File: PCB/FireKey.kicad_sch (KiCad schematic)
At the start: 76 parts, among them SW1 SW_MEC_5E, U1 Arduino_Pro_Micro_USB-C

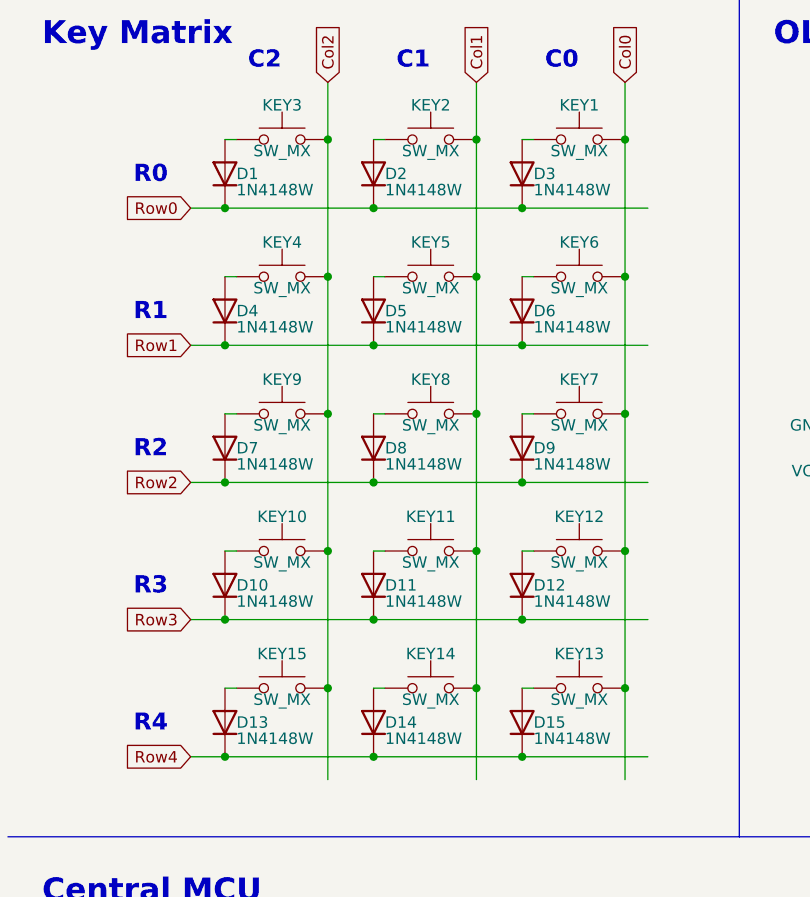
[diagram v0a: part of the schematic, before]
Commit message: fixed diode naming in schematic
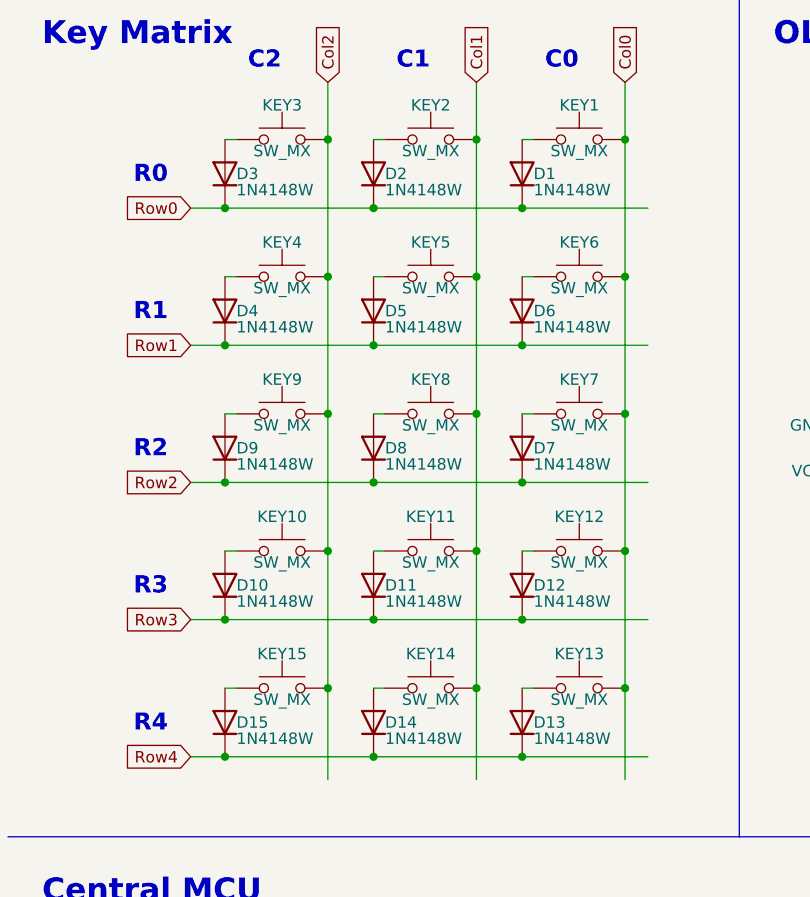
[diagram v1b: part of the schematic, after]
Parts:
- renumbered D3 to D1, D15 to D13, D13 to D15, D1 to D3, D9 to D7, D7 to D9
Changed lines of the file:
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@@
   (symbol (lib_id "Device:D") (at 36.83 64.77 90) (unit 1)
     (in_bom yes) (on_board yes)
-    (property "Reference" "D7" (id 0) (at 38.1 64.77 90)
+    (property "Reference" "D9" (id 0) (at 38.1 64.77 90)
       (effects (font (size 1.27 1.27)) (justify right))
     )
@@
   (symbol (lib_id "Device:D") (at 69.85 64.77 90) (unit 1)
     (in_bom yes) (on_board yes)
-    (property "Reference" "D9" (id 0) (at 71.12 64.77 90)
+    (property "Reference" "D7" (id 0) (at 71.12 64.77 90)
       (effects (font (size 1.27 1.27)) (justify right))
     )
@@
   (symbol (lib_id "Device:D") (at 36.83 95.25 90) (unit 1)
     (in_bom yes) (on_board yes)
-    (property "Reference" "D13" (id 0) (at 38.1 95.25 90)
+    (property "Reference" "D15" (id 0) (at 38.1 95.25 90)
       (effects (font (size 1.27 1.27)) (justify right))
     )
@@
   (symbol (lib_id "Device:D") (at 69.85 34.29 90) (unit 1)
     (in_bom yes) (on_board yes)
-    (property "Reference" "D3" (id 0) (at 71.12 34.29 90)
+    (property "Reference" "D1" (id 0) (at 71.12 34.29 90)
       (effects (font (size 1.27 1.27)) (justify right))
     )
@@
   (symbol (lib_id "Device:D") (at 69.85 95.25 90) (unit 1)
     (in_bom yes) (on_board yes)
-    (property "Reference" "D15" (id 0) (at 71.12 95.25 90)
+    (property "Reference" "D13" (id 0) (at 71.12 95.25 90)
       (effects (font (size 1.27 1.27)) (justify right))
     )
@@
   (symbol (lib_id "Device:D") (at 36.83 34.29 90) (unit 1)
     (in_bom yes) (on_board yes)
-    (property "Reference" "D1" (id 0) (at 38.1 34.29 90)
+    (property "Reference" "D3" (id 0) (at 38.1 34.29 90)
       (effects (font (size 1.27 1.27)) (justify right))
     )
@@
       (reference "C15") (unit 1) (value "100nF") (footprint "Capacitor_SMD:C_0603_1608Metric_Pad1.08x0.95mm_HandSolder")
     )
-    (path "/f34b1302-aa97-4813-9c4e-2a8138dd0fb2"
+    (path "/bfd96171-12af-4791-ab58-317d035aa543"
       (reference "D1") (unit 1) (value "1N4148W") (footprint "Diode_SMD:D_SOD-123")
     )
@@
       (reference "D2") (unit 1) (value "1N4148W") (footprint "Diode_SMD:D_SOD-123")
     )
-    (path "/bfd96171-12af-4791-ab58-317d035aa543"
+    (path "/f34b1302-aa97-4813-9c4e-2a8138dd0fb2"
       (reference "D3") (unit 1) (value "1N4148W") (footprint "Diode_SMD:D_SOD-123")
     )
@@
       (reference "D6") (unit 1) (value "1N4148W") (footprint "Diode_SMD:D_SOD-123")
     )
-    (path "/2c55b189-9010-424a-b20d-57c20a3668f7"
+    (path "/56ad33f8-70ed-48d2-b08e-3210a82c8223"
       (reference "D7") (unit 1) (value "1N4148W") (footprint "Diode_SMD:D_SOD-123")
     )
@@
       (reference "D8") (unit 1) (value "1N4148W") (footprint "Diode_SMD:D_SOD-123")
     )
-    (path "/56ad33f8-70ed-48d2-b08e-3210a82c8223"
+    (path "/2c55b189-9010-424a-b20d-57c20a3668f7"
       (reference "D9") (unit 1) (value "1N4148W") (footprint "Diode_SMD:D_SOD-123")
     )
@@
       (reference "D12") (unit 1) (value "1N4148W") (footprint "Diode_SMD:D_SOD-123")
     )
-    (path "/bb947126-6a07-4e0f-b955-2a81a21f7c79"
+    (path "/c8ff5777-16c4-4cc5-b626-563164697ef6"
       (reference "D13") (unit 1) (value "1N4148W") (footprint "Diode_SMD:D_SOD-123")
     )
@@
       (reference "D14") (unit 1) (value "1N4148W") (footprint "Diode_SMD:D_SOD-123")
     )
-    (path "/c8ff5777-16c4-4cc5-b626-563164697ef6"
+    (path "/bb947126-6a07-4e0f-b955-2a81a21f7c79"
       (reference "D15") (unit 1) (value "1N4148W") (footprint "Diode_SMD:D_SOD-123")
     )

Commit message: fixed mx switches
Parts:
- KEY1, KEY10, KEY11, KEY12, KEY13, KEY14, KEY15, KEY2, KEY3, KEY4, KEY5, KEY6, KEY7, KEY8, KEY9: symbol Switch:SW_MEC_5G -> Custom_Parts:SW_MX_1u
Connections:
- net Col0: now also KEY1.2 (A), KEY12.2 (A), KEY13.2 (A), KEY6.2 (A), KEY7.2 (A); no longer KEY1.3 (B), KEY1.4 (B), KEY12.3 (B), KEY12.4 (B), KEY13.3 (B), KEY13.4 (B), KEY6.3 (B), KEY6.4 (B), KEY7.3 (B), KEY7.4 (B)
- net Col1: now also KEY11.2 (A), KEY14.2 (A), KEY2.2 (A), KEY5.2 (A), KEY8.2 (A); no longer KEY11.3 (B), KEY11.4 (B), KEY14.3 (B), KEY14.4 (B), KEY2.3 (B), KEY2.4 (B), KEY5.3 (B), KEY5.4 (B), KEY8.3 (B), KEY8.4 (B)
- net Col2: now also KEY10.2 (A), KEY15.2 (A), KEY3.2 (A), KEY4.2 (A), KEY9.2 (A); no longer KEY10.3 (B), KEY10.4 (B), KEY15.3 (B), KEY15.4 (B), KEY3.3 (B), KEY3.4 (B), KEY4.3 (B), KEY4.4 (B), KEY9.3 (B), KEY9.4 (B)
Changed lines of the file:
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@@
     )
   )
-  (symbol (lib_id "Switch:SW_MEC_5G") (at 59.69 60.96 0) (unit 1)
+  (symbol (lib_name "SW_MX_1u_4") (lib_id "Custom_Parts:SW_MX_1u") (at 59.69 60.96 0) (unit 1)
     (in_bom yes) (on_board yes)
     (property "Reference" "KEY8" (id 0) (at 59.69 57.15 0))
@@
     )
     (pin "1")
-    (pin "3")
-    (pin "2")
-    (pin "4")
+    (pin "2")
+    (pin "2")
   )
   (symbol (lib_id "Device:C") (at 275.59 93.98 0) (unit 1)
@@
     (pin "2")
   )
-  (symbol (lib_id "Switch:SW_MEC_5G") (at 59.69 76.2 0) (unit 1)
+  (symbol (lib_name "SW_MX_1u_5") (lib_id "Custom_Parts:SW_MX_1u") (at 59.69 76.2 0) (unit 1)
     (in_bom yes) (on_board yes)
     (property "Reference" "KEY11" (id 0) (at 59.69 72.39 0))
@@
     )
     (pin "1")
-    (pin "3")
-    (pin "2")
-    (pin "4")
+    (pin "2")
+    (pin "2")
   )
   (symbol (lib_id "Device:D") (at 69.85 80.01 90) (unit 1)
@@
     (pin "2")
   )
-  (symbol (lib_id "Switch:SW_MEC_5G") (at 76.2 60.96 0) (unit 1)
+  (symbol (lib_name "SW_MX_1u_14") (lib_id "Custom_Parts:SW_MX_1u") (at 76.2 60.96 0) (unit 1)
     (in_bom yes) (on_board yes)
     (property "Reference" "KEY7" (id 0) (at 76.2 57.15 0))
@@
     )
     (pin "1")
-    (pin "3")
-    (pin "2")
-    (pin "4")
+    (pin "2")
+    (pin "2")
   )
   (symbol (lib_id "Device:C") (at 275.59 78.74 0) (unit 1)
@@
     (pin "2")
   )
-  (symbol (lib_id "Switch:SW_MEC_5G") (at 43.18 91.44 0) (unit 1)
+  (symbol (lib_name "SW_MX_1u_7") (lib_id "Custom_Parts:SW_MX_1u") (at 43.18 91.44 0) (unit 1)
     (in_bom yes) (on_board yes)
     (property "Reference" "KEY15" (id 0) (at 43.18 87.63 0))
@@
     )
     (pin "1")
-    (pin "3")
-    (pin "2")
-    (pin "4")
+    (pin "2")
+    (pin "2")
   )
   (symbol (lib_id "Device:C") (at 257.81 63.5 0) (unit 1)
@@
     (pin "4")
   )
-  (symbol (lib_id "Switch:SW_MEC_5G") (at 59.69 30.48 0) (unit 1)
+  (symbol (lib_name "SW_MX_1u_13") (lib_id "Custom_Parts:SW_MX_1u") (at 59.69 30.48 0) (unit 1)
     (in_bom yes) (on_board yes)
     (property "Reference" "KEY2" (id 0) (at 59.69 26.67 0))
@@
     )
     (pin "1")
-    (pin "3")
-    (pin "2")
-    (pin "4")
-  )
-  (symbol (lib_id "Switch:SW_MEC_5G") (at 43.18 30.48 0) (unit 1)
+    (pin "2")
+    (pin "2")
+  )
+  (symbol (lib_name "SW_MX_1u_12") (lib_id "Custom_Parts:SW_MX_1u") (at 43.18 30.48 0) (unit 1)
     (in_bom yes) (on_board yes)
     (property "Reference" "KEY3" (id 0) (at 43.18 26.67 0))
@@
     )
     (pin "1")
-    (pin "3")
-    (pin "2")
-    (pin "4")
+    (pin "2")
+    (pin "2")
   )
   (symbol (lib_id "Device:D") (at 69.85 64.77 90) (unit 1)
@@
     (pin "4")
   )
-  (symbol (lib_id "Switch:SW_MEC_5G") (at 43.18 60.96 0) (unit 1)
+  (symbol (lib_name "SW_MX_1u_3") (lib_id "Custom_Parts:SW_MX_1u") (at 43.18 60.96 0) (unit 1)
     (in_bom yes) (on_board yes)
     (property "Reference" "KEY9" (id 0) (at 43.18 57.15 0))
@@
     )
     (pin "1")
-    (pin "3")
-    (pin "2")
-    (pin "4")
+    (pin "2")
+    (pin "2")
   )
   (symbol (lib_id "power:GND") (at 273.05 149.86 90) (unit 1)
@@
     (pin "1")
   )
-  (symbol (lib_id "Switch:SW_MEC_5G") (at 76.2 76.2 0) (unit 1)
+  (symbol (lib_name "SW_MX_1u_6") (lib_id "Custom_Parts:SW_MX_1u") (at 76.2 76.2 0) (unit 1)
     (in_bom yes) (on_board yes)
     (property "Reference" "KEY12" (id 0) (at 76.2 72.39 0))
@@
     )
     (pin "1")
-    (pin "3")
-    (pin "2")
-    (pin "4")
-  )
-  (symbol (lib_id "Switch:SW_MEC_5G") (at 43.18 76.2 0) (unit 1)
+    (pin "2")
+    (pin "2")
+  )
+  (symbol (lib_name "SW_MX_1u_2") (lib_id "Custom_Parts:SW_MX_1u") (at 43.18 76.2 0) (unit 1)
     (in_bom yes) (on_board yes)
     (property "Reference" "KEY10" (id 0) (at 43.18 72.39 0))
@@
     )
     (pin "1")
-    (pin "3")
-    (pin "2")
-    (pin "4")
+    (pin "2")
+    (pin "2")
   )
   (symbol (lib_id "Device:C") (at 266.7 33.02 0) (unit 1)
@@
     (pin "1")
   )
-  (symbol (lib_id "Switch:SW_MEC_5G") (at 59.69 45.72 0) (unit 1)
+  (symbol (lib_name "SW_MX_1u_10") (lib_id "Custom_Parts:SW_MX_1u") (at 59.69 45.72 0) (unit 1)
     (in_bom yes) (on_board yes)
     (property "Reference" "KEY5" (id 0) (at 59.69 41.91 0))
@@
     )
     (pin "1")
-    (pin "3")
-    (pin "2")
-    (pin "4")
-  )
-  (symbol (lib_id "Switch:SW_MEC_5G") (at 43.18 45.72 0) (unit 1)
+    (pin "2")
+    (pin "2")
+  )
+  (symbol (lib_name "SW_MX_1u_11") (lib_id "Custom_Parts:SW_MX_1u") (at 43.18 45.72 0) (unit 1)
     (in_bom yes) (on_board yes)
     (property "Reference" "KEY4" (id 0) (at 43.18 41.91 0))
@@
     )
     (pin "1")
-    (pin "3")
-    (pin "2")
-    (pin "4")
+    (pin "2")
+    (pin "2")
   )
   (symbol (lib_id "power:VCC") (at 254 90.17 90) (unit 1)
@@
     (pin "2")
   )
-  (symbol (lib_id "Switch:SW_MEC_5G") (at 59.69 91.44 0) (unit 1)
+  (symbol (lib_name "SW_MX_1u_8") (lib_id "Custom_Parts:SW_MX_1u") (at 59.69 91.44 0) (unit 1)
     (in_bom yes) (on_board yes)
     (property "Reference" "KEY14" (id 0) (at 59.69 87.63 0))
@@
     )
     (pin "1")
-    (pin "3")
-    (pin "2")
-    (pin "4")
+    (pin "2")
+    (pin "2")
   )
   (symbol (lib_id "Custom_Parts:DY-S352818{slash}6812-2T") (at 213.36 48.26 0) (mirror x) (unit 1)
@@
     (pin "1")
   )
-  (symbol (lib_id "Switch:SW_MEC_5G") (at 76.2 45.72 0) (unit 1)
+  (symbol (lib_id "Custom_Parts:SW_MX_1u") (at 76.2 45.72 0) (unit 1)
     (in_bom yes) (on_board yes)
     (property "Reference" "KEY6" (id 0) (at 76.2 41.91 0))
@@
     )
     (pin "1")
-    (pin "3")
-    (pin "2")
-    (pin "4")
+    (pin "2")
+    (pin "2")
   )
   (symbol (lib_id "power:VCC") (at 219.71 25.4 270) (mirror x) (unit 1)
@@
     (pin "1")
   )
-  (symbol (lib_id "Switch:SW_MEC_5G") (at 76.2 91.44 0) (unit 1)
+  (symbol (lib_name "SW_MX_1u_9") (lib_id "Custom_Parts:SW_MX_1u") (at 76.2 91.44 0) (unit 1)
     (in_bom yes) (on_board yes)
     (property "Reference" "KEY13" (id 0) (at 76.2 87.63 0))
@@
     )
     (pin "1")
-    (pin "3")
-    (pin "2")
-    (pin "4")
+    (pin "2")
+    (pin "2")
   )
   (symbol (lib_id "Custom_Parts:DY-S352818{slash}6812-2T") (at 213.36 78.74 0) (mirror x) (unit 1)
@@
     (pin "2")
   )
-  (symbol (lib_id "Switch:SW_MEC_5G") (at 76.2 30.48 0) (unit 1)
+  (symbol (lib_name "SW_MX_1u_1") (lib_id "Custom_Parts:SW_MX_1u") (at 76.2 30.48 0) (unit 1)
     (in_bom yes) (on_board yes)
     (property "Reference" "KEY1" (id 0) (at 76.2 26.67 0))
@@
     )
     (pin "1")
-    (pin "3")
-    (pin "2")
-    (pin "4")
+    (pin "2")
+    (pin "2")
   )
   (symbol (lib_id "power:GND") (at 127 62.23 270) (unit 1)

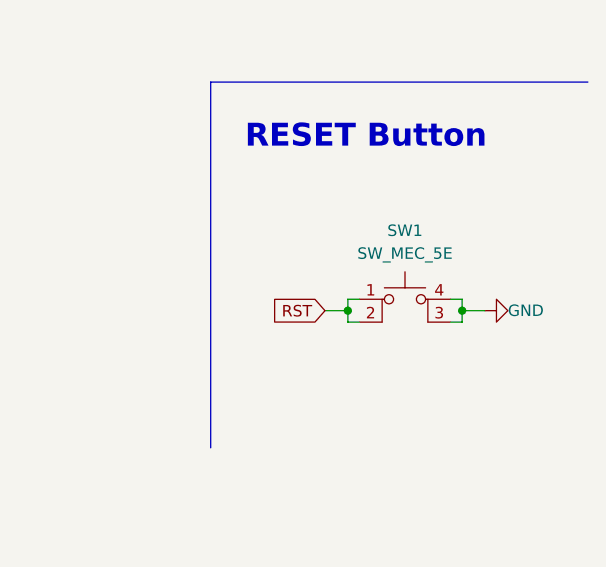
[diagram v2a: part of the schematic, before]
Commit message: fixed rst switch
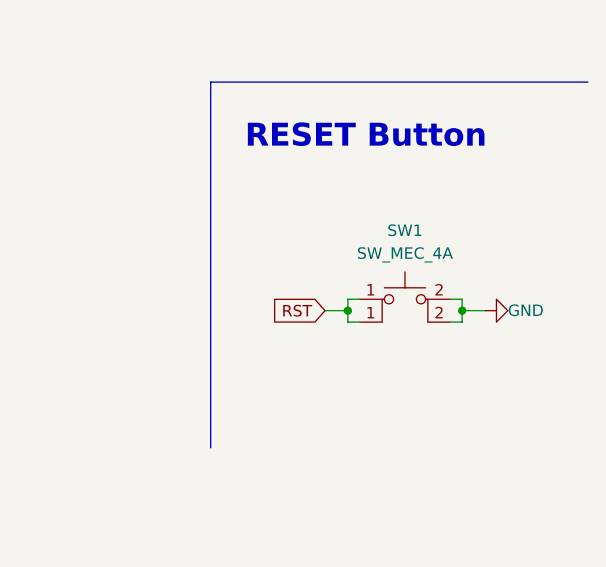
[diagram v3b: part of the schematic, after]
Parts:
- SW1: value SW_MEC_5E -> SW_MEC_4A; symbol Switch:SW_MEC_5E -> Custom_Parts:SW_MEC_4A
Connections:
- net GND: now also SW1.2; no longer SW1.3 (K), SW1.4 (A)
- net RST: no longer SW1.2
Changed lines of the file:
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@@
     (pin "2")
   )
-  (symbol (lib_id "Switch:SW_MEC_5E") (at 264.16 151.13 0) (unit 1)
+  (symbol (lib_id "Custom_Parts:SW_MEC_4A") (at 264.16 151.13 0) (unit 1)
     (in_bom yes) (on_board yes) (fields_autoplaced)
     (property "Reference" "SW1" (id 0) (at 264.16 140.97 0))
-    (property "Value" "SW_MEC_5E" (id 1) (at 264.16 143.51 0))
+    (property "Value" "SW_MEC_4A" (id 1) (at 264.16 143.51 0))
     (property "Footprint" "Button_Switch_SMD:SW_SPST_TL3342" (id 2) (at 264.16 143.51 0)
       (effects (font (size 1.27 1.27)) hide)
@@
     )
     (pin "1")
-    (pin "2")
-    (pin "3")
-    (pin "4")
+    (pin "1")
+    (pin "2")
+    (pin "2")
   )
   (symbol (lib_id "Device:D") (at 69.85 95.25 90) (unit 1)
@@
     )
     (path "/c7b5504d-1a0d-40d4-ad19-3310d0f5f11d"
-      (reference "SW1") (unit 1) (value "SW_MEC_5E") (footprint "Button_Switch_SMD:SW_SPST_TL3342")
+      (reference "SW1") (unit 1) (value "SW_MEC_4A") (footprint "Button_Switch_SMD:SW_SPST_TL3342")
     )
     (path "/051f7d79-ef19-4f53-afce-cb909f526a33"

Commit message: worked on DRC errors
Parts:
- removed H1, H4: Pad, TestPoint:TestPoint_Pad_D2.5mm, symbol Mechanical:MountingHole_Pad
- D1, D10, D11, D12, D13, D14, D15, D2, D3, D4, D5, D6, D7, D8, D9: footprint Diode_SMD:D_SOD-123 -> Custom_Parts:D_SOD-123
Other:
- moved on the sheet: H3
